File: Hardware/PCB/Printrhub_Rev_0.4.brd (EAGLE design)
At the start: 82.5 x 61.2 mm, 72 parts, among them J1 DM3D-SF, SW1 SPST_TACT-KMR2, SW2 SPST_TACT-KMR2, U1 MK20DX256VLH7, U2 AP1117E, U3 MAX308-SOT23, Y2 16Mhz/8pF

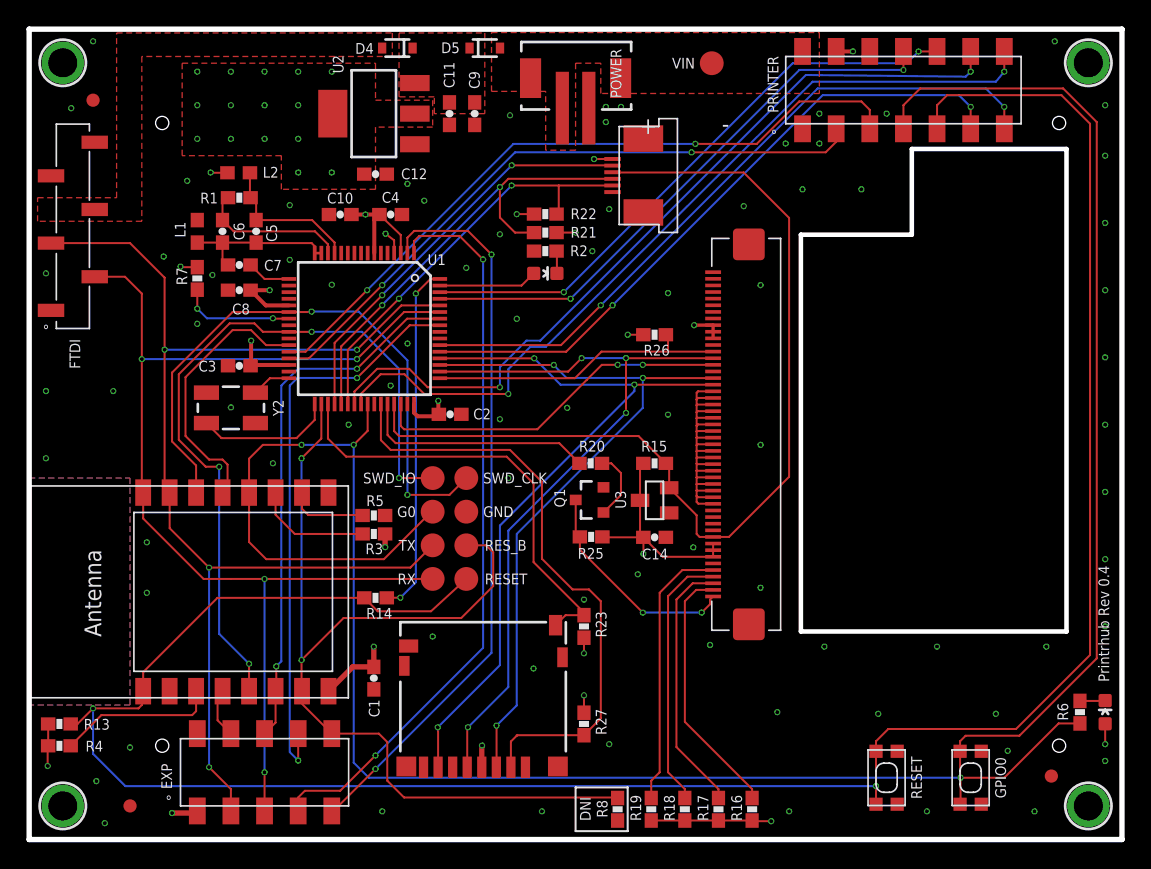
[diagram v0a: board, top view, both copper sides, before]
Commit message: Readded SCL1 and SDA1 (so this version is committed, too).
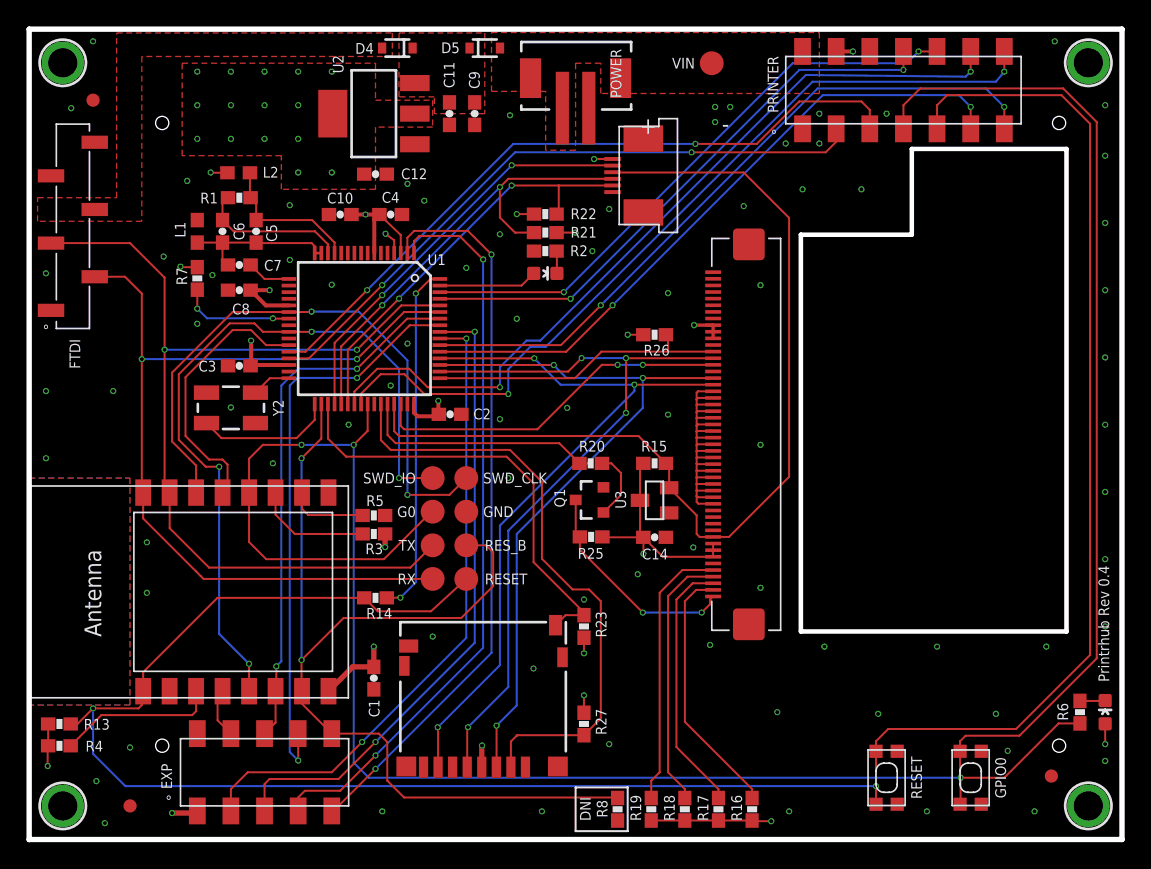
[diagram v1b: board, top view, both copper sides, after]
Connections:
- net SCL1: now also JP2.3
- net SDA1: now also JP2.5
- net UART2_RX: no longer JP2.5
- net UART2_TX: no longer JP2.3
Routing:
- net SCL1: track 0.00 -> 48.8 mm, vias 0 -> 2
- net SDA1: track 0.00 -> 48.5 mm, vias 0 -> 2
- net UART2_TX: track 92.2 -> 73.2 mm, vias 4 -> 2
- net UART2_RX: track 86.8 -> 69.3 mm, vias 4 -> 2
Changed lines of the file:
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@@
 <contactref element="JP2" pad="2"/>
 <via x="3.175" y="55.245" extent="1-16" drill="0.2794"/>
-<via x="43.561" y="55.34" extent="1-16" drill="0.2794"/>
+<via x="51.816" y="55.34" extent="1-16" drill="0.2794"/>
 <via x="57.15" y="52.578" extent="1-16" drill="0.2794"/>
 <via x="27.305" y="34.29" extent="1-16" drill="0.2794"/>
@@
 <via x="5.715" y="1.238" extent="1-16" drill="0.2794"/>
 <via x="62.865" y="49.117" extent="1-16" drill="0.2794"/>
-<via x="43.561" y="54.197" extent="1-16" drill="0.2794"/>
-<via x="44.704" y="55.34" extent="1-16" drill="0.2794"/>
+<via x="51.816" y="54.197" extent="1-16" drill="0.2794"/>
+<via x="52.959" y="55.34" extent="1-16" drill="0.2794"/>
 <via x="59.69" y="52.578" extent="1-16" drill="0.2794"/>
 <via x="64.77" y="54.832" extent="1-16" drill="0.2794"/>
@@
 <wire x1="8.255" y1="26.182" x2="8.611" y2="26.207" width="0.2032" layer="1"/>
 <wire x1="8.611" y1="26.207" x2="8.611" y2="24.25" width="0.1524" layer="1"/>
-<wire x1="8.611" y1="24.25" x2="13.176" y2="19.685" width="0.1524" layer="1"/>
-<wire x1="30.48" y1="19.685" x2="17.78" y2="19.685" width="0.1524" layer="1"/>
-<contactref element="JP2" pad="5"/>
-<wire x1="15.24" y1="19.685" x2="13.176" y2="19.685" width="0.1524" layer="1"/>
-<wire x1="17.78" y1="2.159" x2="17.78" y2="5.08" width="0.1524" layer="1"/>
-<via x="17.78" y="5.08" extent="1-16" drill="0.2794"/>
-<wire x1="17.78" y1="5.08" x2="17.78" y2="19.685" width="0.1524" layer="16"/>
-<via x="17.78" y="19.685" extent="1-16" drill="0.2794"/>
-<wire x1="17.78" y1="19.685" x2="15.24" y2="19.685" width="0.1524" layer="1"/>
+<wire x1="8.611" y1="24.25" x2="12.6205" y2="20.2405" width="0.1524" layer="1"/>
+<wire x1="12.6205" y1="20.2405" x2="12.954" y2="19.907" width="0.1524" layer="1"/>
+<wire x1="30.48" y1="19.685" x2="13.176" y2="19.685" width="0.1524" layer="1"/>
+<wire x1="13.176" y1="19.685" x2="12.954" y2="19.907" width="0.1524" layer="1"/>
 </signal>
 <signal name="UART2_TX">
@@
 <wire x1="10.16" y1="26.137" x2="10.611" y2="26.207" width="0.2032" layer="1"/>
 <wire x1="10.611" y1="26.207" x2="10.611" y2="23.52" width="0.1524" layer="1"/>
+<wire x1="10.611" y1="23.52" x2="13.589" y2="20.542" width="0.1524" layer="1"/>
 <wire x1="10.23" y1="37.0012" x2="10.23" y2="26.588" width="0.1524" layer="1"/>
 <wire x1="10.23" y1="26.588" x2="10.611" y2="26.207" width="0.1524" layer="1"/>
 <wire x1="28.797" y1="20.542" x2="30.48" y2="22.225" width="0.1524" layer="1"/>
-<contactref element="JP2" pad="3"/>
-<wire x1="15.24" y1="2.159" x2="15.24" y2="3.81" width="0.1524" layer="1"/>
-<wire x1="15.24" y1="3.81" x2="13.589" y2="5.461" width="0.1524" layer="1"/>
-<via x="13.589" y="5.461" extent="1-16" drill="0.2794"/>
-<wire x1="13.589" y1="5.461" x2="13.589" y2="20.542" width="0.1524" layer="16"/>
-<via x="13.589" y="20.542" extent="1-16" drill="0.2794"/>
-<wire x1="13.589" y1="20.542" x2="10.611" y2="23.52" width="0.1524" layer="1"/>
 </signal>
 <signal name="PRINTER_RTS">
@@
 <signal name="SCL1">
 <contactref element="U1" pad="55"/>
+<contactref element="JP2" pad="3"/>
+<wire x1="31.02" y1="37.847" x2="33.019" y2="37.847" width="0.1524" layer="1"/>
+<wire x1="33.019" y1="37.847" x2="33.02" y2="37.846" width="0.1524" layer="1"/>
+<via x="33.02" y="37.846" extent="1-16" drill="0.2794"/>
+<wire x1="33.02" y1="37.846" x2="33.02" y2="15.24" width="0.1524" layer="16"/>
+<wire x1="33.02" y1="15.24" x2="25.146" y2="7.366" width="0.1524" layer="16"/>
+<via x="25.146" y="7.366" extent="1-16" drill="0.2794"/>
+<wire x1="25.146" y1="7.366" x2="22.86" y2="5.08" width="0.1524" layer="1"/>
+<wire x1="22.86" y1="5.08" x2="16.51" y2="5.08" width="0.1524" layer="1"/>
+<wire x1="15.24" y1="2.159" x2="15.24" y2="3.81" width="0.1524" layer="1"/>
+<wire x1="15.24" y1="3.81" x2="16.51" y2="5.08" width="0.1524" layer="1"/>
 </signal>
 <signal name="SDA1">
 <contactref element="U1" pad="56"/>
+<contactref element="JP2" pad="5"/>
+<wire x1="17.78" y1="2.159" x2="17.78" y2="4.191" width="0.1524" layer="1"/>
+<wire x1="17.78" y1="4.191" x2="18.161" y2="4.572" width="0.1524" layer="1"/>
+<wire x1="18.161" y1="4.572" x2="23.368" y2="4.572" width="0.1524" layer="1"/>
+<wire x1="23.368" y1="4.572" x2="26.162" y2="7.366" width="0.1524" layer="1"/>
+<via x="26.162" y="7.366" extent="1-16" drill="0.2794"/>
+<wire x1="26.162" y1="7.366" x2="33.655" y2="14.859" width="0.1524" layer="16"/>
+<wire x1="33.655" y1="14.859" x2="33.655" y2="38.354" width="0.1524" layer="16"/>
+<wire x1="31.02" y1="38.347" x2="33.648" y2="38.347" width="0.1524" layer="1"/>
+<wire x1="33.648" y1="38.347" x2="33.655" y2="38.354" width="0.1524" layer="1"/>
+<via x="33.655" y="38.354" extent="1-16" drill="0.2794"/>
 </signal>
 </signals>

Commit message: Added pull-up and pull-down resistors for PRINTER_RESET and PRINTER_ERASE signals. Replaced plated mounting holes with larger holes (without plate). Moved a few parts for nicer layout.
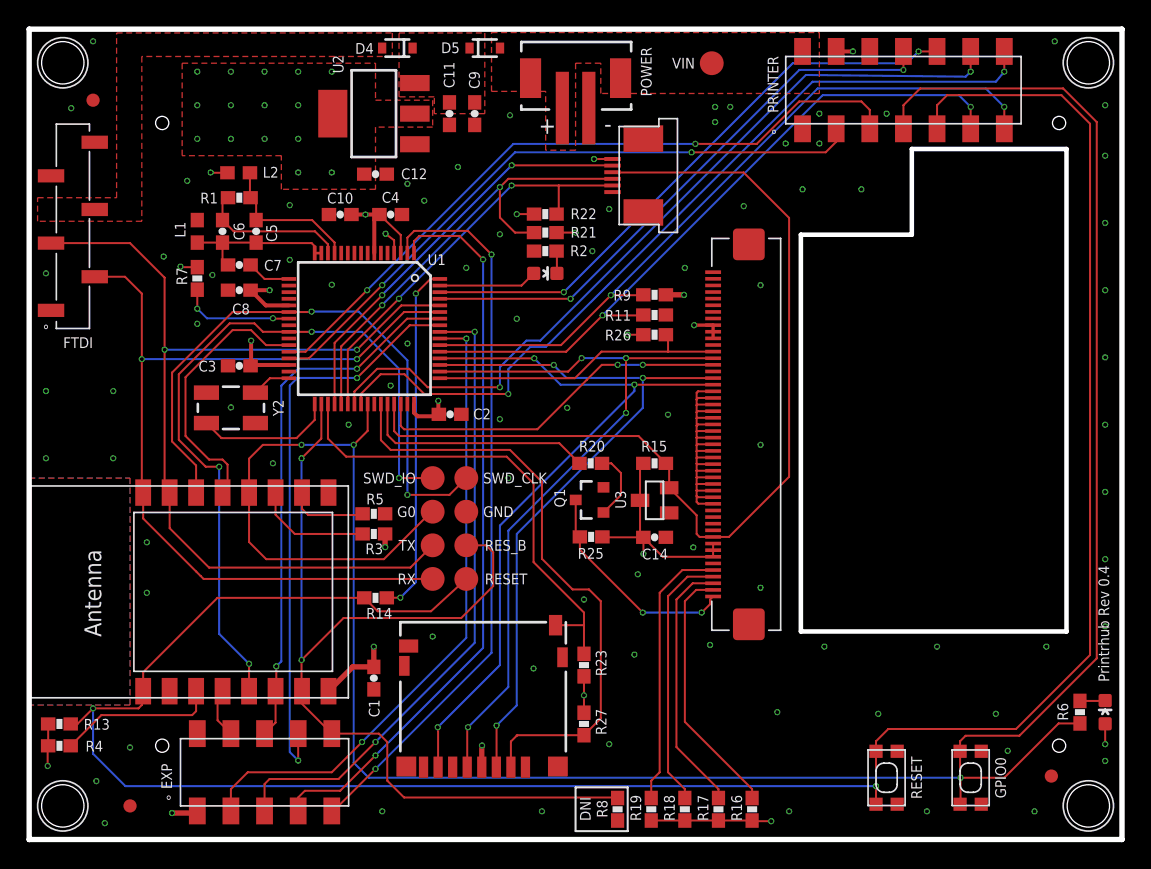
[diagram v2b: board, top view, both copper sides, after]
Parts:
- added R11, R9: 10K, appfruits:0603-RES
- U$15, U$16, U$17, U$18: value MOUNTINGHOLE2.0 -> MOUNTINGHOLE; device microbuilder:MOUNTINGHOLE_2.0_PLATED -> appfruits:HOLE_M3.0
- moved R23 2.92 mm to (41.9, 13.2)
- moved R5 0.13 mm to (26.0, 24.6)
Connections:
- net 3.3V: now also R9.2
- net GND: now also R11.1
- net PRINTER_ERASE: now also R11.2
- net PRINTER_RESET: now also R9.1
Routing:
- net PRINTER_ERASE: track 50.1 -> 53.2 mm
- net SD_CARD_DETECT: track 33.5 -> 36.1 mm
- net PRINTER_RESET: track 52.9 -> 55.4 mm
- net 3.3V: track 78.3 -> 79.9 mm
- net GND: vias 80 -> 83
